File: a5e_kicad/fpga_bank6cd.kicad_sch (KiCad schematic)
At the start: 1 part, among them U7 A5EB013B-B23B

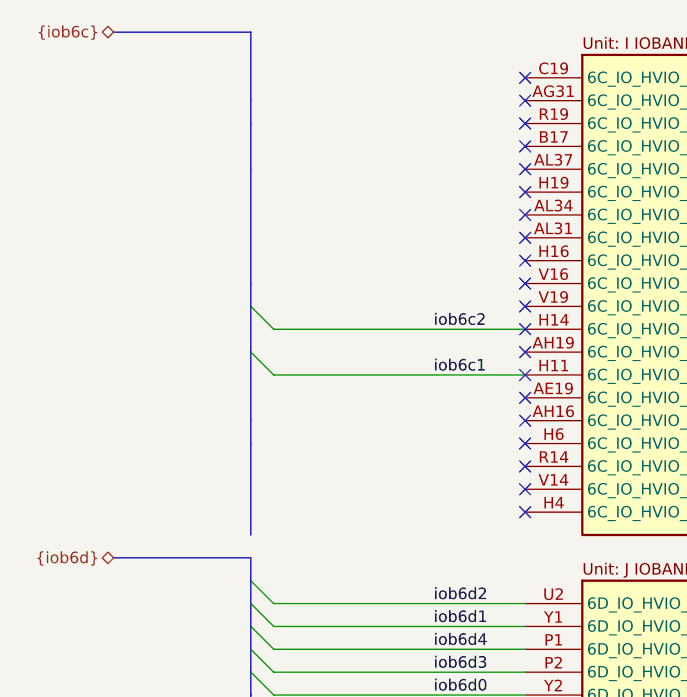
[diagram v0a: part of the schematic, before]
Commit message: Schematic reorg step 9: ERC to zero
- Wires trimmed back to their last label or cap (SDM config lines, LPDDR4
  decoupling rows, PG pins); loose stubs and R29 leftovers removed
- Unused bus links removed: {iob6a}, {iobank_2aB}, {iob6c}, {phy} and the
  io_headers {jtag} (sheet pins, root buses, unnamed internal buses);
  {iob6b} bus tail trimmed

Netdiff: 0 renamed, 0 connectivity diffs. ERC 21 -> 0. PCB unchanged, DRC parity 0.
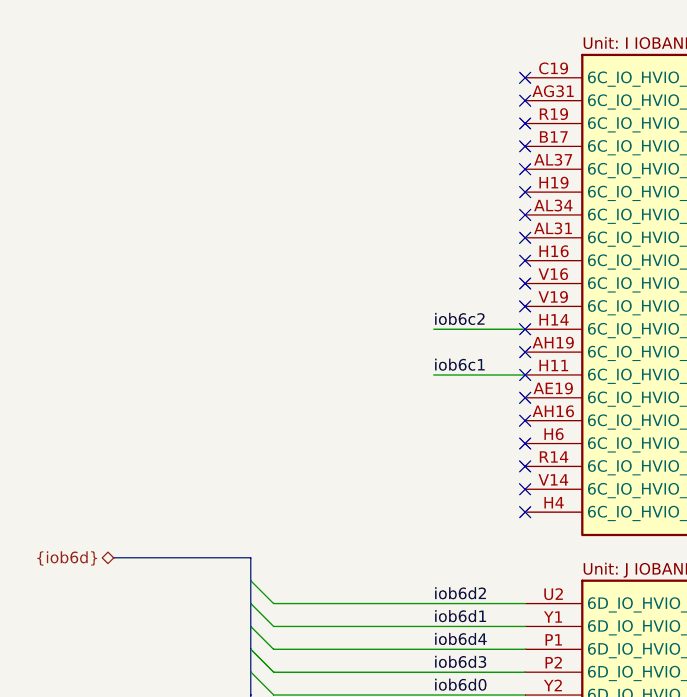
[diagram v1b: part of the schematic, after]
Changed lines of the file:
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@@
-	)
-	(bus_entry
-		(at 66.04 58.42)
-		(size 2.54 2.54)
-		(stroke
-			(width 0)
-			(type default)
-		)
-	)
-	(bus_entry
-		(at 66.04 53.34)
-		(size 2.54 2.54)
-		(stroke
-			(width 0)
-			(type default)
-		)
 	)
 	(bus_entry
@@
 	(bus
 		(pts
-			(xy 66.04 50.8) (xy 66.04 53.34)
-		)
-		(stroke
-			(width 0)
-			(type default)
-		)
-	)
-	(bus
-		(pts
 			(xy 66.04 121.92) (xy 66.04 124.46)
 		)
@@
 		)
 	)
-	(bus
-		(pts
-			(xy 66.04 58.42) (xy 66.04 66.04)
-		)
-		(stroke
-			(width 0)
-			(type default)
-		)
-	)
-	(bus
-		(pts
-			(xy 66.04 38.1) (xy 66.04 50.8)
-		)
-		(stroke
-			(width 0)
-			(type default)
-		)
-	)
-	(wire
-		(pts
-			(xy 68.58 60.96) (xy 96.52 60.96)
+	(wire
+		(pts
+			(xy 86.36 60.96) (xy 96.52 60.96)
 		)
 		(stroke
@@
 		)
 	)
-	(bus
-		(pts
-			(xy 50.8 22.86) (xy 66.04 22.86)
-		)
-		(stroke
-			(width 0)
-			(type default)
-		)
-	)
-	(bus
-		(pts
-			(xy 66.04 66.04) (xy 66.04 68.58)
-		)
-		(stroke
-			(width 0)
-			(type default)
-		)
-	)
-	(bus
-		(pts
-			(xy 66.04 33.02) (xy 66.04 38.1)
-		)
-		(stroke
-			(width 0)
-			(type default)
-		)
-	)
 	(wire
 		(pts
@@
 	(wire
 		(pts
-			(xy 68.58 55.88) (xy 96.52 55.88)
+			(xy 86.36 55.88) (xy 96.52 55.88)
 		)
 		(stroke
@@
 	(bus
 		(pts
-			(xy 66.04 22.86) (xy 66.04 30.48)
-		)
-		(stroke
-			(width 0)
-			(type default)
-		)
-	)
-	(bus
-		(pts
 			(xy 66.04 86.36) (xy 66.04 88.9)
 		)
@@
 	(bus
 		(pts
-			(xy 66.04 68.58) (xy 66.04 78.74)
-		)
-		(stroke
-			(width 0)
-			(type default)
-		)
-	)
-	(bus
-		(pts
 			(xy 66.04 99.06) (xy 66.04 101.6)
 		)
@@
 		)
 	)
-	(bus
-		(pts
-			(xy 66.04 30.48) (xy 66.04 33.02)
-		)
-		(stroke
-			(width 0)
-			(type default)
-		)
-	)
 	(wire
 		(pts
@@
 		(pts
 			(xy 66.04 88.9) (xy 66.04 91.44)
-		)
-		(stroke
-			(width 0)
-			(type default)
-		)
-	)
-	(bus
-		(pts
-			(xy 66.04 53.34) (xy 66.04 58.42)
 		)
 		(stroke
@@
 		)
 	)
-	(hierarchical_label "{iob6c}"
-		(shape bidirectional)
-		(at 50.8 22.86 180)
-		(effects
-			(font
-				(size 1.27 1.27)
-			)
-			(justify right)
-		)
-	)

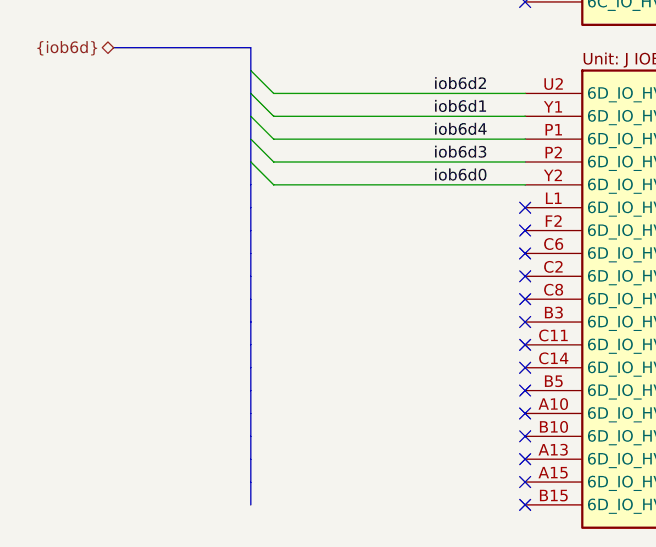
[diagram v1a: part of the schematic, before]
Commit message: Ethernet PHY passives to 0201, R27/R28 to 0402, preliminary RGMII routing
- 31 PHY passives on the hps_ethernet sheet 0402 -> 0201 (C24 22u stays
  0402): 100n C190183, 1u C272877, 27p C85899, 10k C473048,
  330R C516485, 4K7 C270346, 1K5 C270361, 2K49 C473476.
- Refclk bias R27/R28 0201 -> 0402 (C25120, 49.9R); R28 moved 0.1 mm
  to +x to clear the refclk_N meander.
- Preliminary RGMII routing: RX on F.Cu, TX on In2. Group spread
  TX 79 ps (TXD1 longest), RX 44 ps.
- Schematic sheets as saved by eeschema.
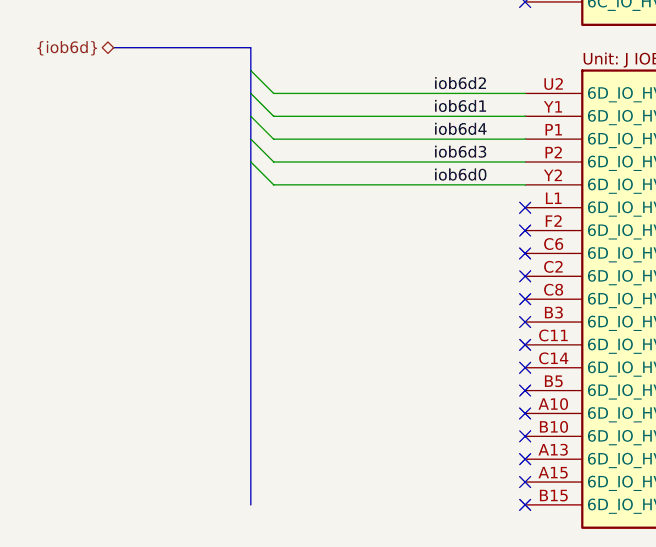
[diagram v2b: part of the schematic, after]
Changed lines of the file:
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@@
 	)
 	(no_connect
-		(at 96.52 27.94)
+		(at 96.52 38.1)
 	)
 	(no_connect
-		(at 96.52 48.26)
+		(at 96.52 129.54)
 	)
 	(no_connect
-		(at 96.52 38.1)
+		(at 96.52 66.04)
 	)
 	(no_connect
-		(at 96.52 66.04)
+		(at 96.52 127)
 	)
 	(no_connect
@@
 	)
 	(no_connect
+		(at 96.52 104.14)
+	)
+	(no_connect
+		(at 96.52 109.22)
+	)
+	(no_connect
+		(at 96.52 48.26)
+	)
+	(no_connect
 		(at 96.52 50.8)
 	)
 	(no_connect
+		(at 96.52 71.12)
+	)
+	(no_connect
+		(at 96.52 99.06)
+	)
+	(no_connect
+		(at 96.52 33.02)
+	)
+	(no_connect
+		(at 96.52 27.94)
+	)
+	(no_connect
 		(at 96.52 60.96)
 	)
 	(no_connect
+		(at 96.52 101.6)
+	)
+	(no_connect
+		(at 96.52 68.58)
+	)
+	(no_connect
+		(at 96.52 132.08)
+	)
+	(no_connect
+		(at 96.52 121.92)
+	)
+	(no_connect
+		(at 96.52 40.64)
+	)
+	(no_connect
+		(at 96.52 114.3)
+	)
+	(no_connect
 		(at 96.52 76.2)
 	)
 	(no_connect
+		(at 96.52 119.38)
+	)
+	(no_connect
+		(at 96.52 35.56)
+	)
+	(no_connect
+		(at 96.52 116.84)
+	)
+	(no_connect
+		(at 96.52 53.34)
+	)
+	(no_connect
 		(at 96.52 73.66)
 	)
 	(no_connect
+		(at 96.52 124.46)
+	)
+	(no_connect
 		(at 96.52 58.42)
 	)
@@
 		(at 96.52 45.72)
 	)
+	(no_connect
+		(at 96.52 111.76)
+	)
+	(no_connect
+		(at 96.52 106.68)
+	)
 	(bus_entry
 		(at 66.04 86.36)
@@
 	(bus
 		(pts
-			(xy 66.04 121.92) (xy 66.04 124.46)
-		)
-		(stroke
-			(width 0)
-			(type default)
-		)
-	)
-	(bus
-		(pts
 			(xy 50.8 81.28) (xy 66.04 81.28)
 		)
@@
 	(bus
 		(pts
-			(xy 66.04 127) (xy 66.04 129.54)
-		)
-		(stroke
-			(width 0)
-			(type default)
-		)
-	)
-	(bus
-		(pts
-			(xy 66.04 119.38) (xy 66.04 121.92)
-		)
-		(stroke
-			(width 0)
-			(type default)
-		)
-	)
-	(bus
-		(pts
 			(xy 66.04 81.28) (xy 66.04 83.82)
 		)
@@
 	(bus
 		(pts
-			(xy 66.04 129.54) (xy 66.04 132.08)
-		)
-		(stroke
-			(width 0)
-			(type default)
-		)
-	)
-	(bus
-		(pts
-			(xy 66.04 101.6) (xy 66.04 104.14)
+			(xy 66.04 93.98) (xy 66.04 132.08)
 		)
 		(stroke
@@
 	(bus
 		(pts
-			(xy 66.04 106.68) (xy 66.04 109.22)
-		)
-		(stroke
-			(width 0)
-			(type default)
-		)
-	)
-	(bus
-		(pts
-			(xy 66.04 104.14) (xy 66.04 106.68)
-		)
-		(stroke
-			(width 0)
-			(type default)
-		)
-	)
-	(bus
-		(pts
 			(xy 66.04 91.44) (xy 66.04 93.98)
 		)
@@
 	(bus
 		(pts
-			(xy 66.04 114.3) (xy 66.04 116.84)
-		)
-		(stroke
-			(width 0)
-			(type default)
-		)
-	)
-	(bus
-		(pts
-			(xy 66.04 93.98) (xy 66.04 96.52)
-		)
-		(stroke
-			(width 0)
-			(type default)
-		)
-	)
-	(bus
-		(pts
 			(xy 66.04 86.36) (xy 66.04 88.9)
 		)
@@
 		)
 	)
-	(bus
-		(pts
-			(xy 66.04 124.46) (xy 66.04 127)
-		)
-		(stroke
-			(width 0)
-			(type default)
-		)
-	)
-	(bus
-		(pts
-			(xy 66.04 99.06) (xy 66.04 101.6)
-		)
-		(stroke
-			(width 0)
-			(type default)
-		)
-	)
-	(bus
-		(pts
-			(xy 66.04 116.84) (xy 66.04 119.38)
-		)
-		(stroke
-			(width 0)
-			(type default)
-		)
-	)
-	(bus
-		(pts
-			(xy 66.04 111.76) (xy 66.04 114.3)
-		)
-		(stroke
-			(width 0)
-			(type default)
-		)
-	)
-	(bus
-		(pts
-			(xy 66.04 96.52) (xy 66.04 99.06)
-		)
-		(stroke
-			(width 0)
-			(type default)
-		)
-	)
-	(bus
-		(pts
-			(xy 66.04 109.22) (xy 66.04 111.76)
-		)
-		(stroke
-			(width 0)
-			(type default)
-		)
-	)
 	(wire
 		(pts
@@
 		)
 	)
-	(no_connect
-		(at 96.52 132.08)
-	)
-	(no_connect
-		(at 96.52 119.38)
-	)
-	(no_connect
-		(at 96.52 124.46)
-	)
-	(no_connect
-		(at 96.52 101.6)
-	)
-	(no_connect
-		(at 96.52 40.64)
-	)
-	(no_connect
-		(at 96.52 127)
-	)
-	(no_connect
-		(at 96.52 33.02)
-	)
-	(no_connect
-		(at 96.52 99.06)
-	)
-	(no_connect
-		(at 96.52 121.92)
-	)
-	(no_connect
-		(at 96.52 109.22)
-	)
-	(no_connect
-		(at 96.52 106.68)
-	)
-	(no_connect
-		(at 96.52 111.76)
-	)
-	(no_connect
-		(at 96.52 116.84)
-	)
-	(no_connect
-		(at 96.52 68.58)
-	)
-	(no_connect
-		(at 96.52 53.34)
-	)
-	(no_connect
-		(at 96.52 35.56)
-	)
-	(no_connect
-		(at 96.52 114.3)
-	)
-	(no_connect
-		(at 96.52 104.14)
-	)
-	(no_connect
-		(at 96.52 129.54)
-	)
-	(no_connect
-		(at 96.52 71.12)
-	)
 )
